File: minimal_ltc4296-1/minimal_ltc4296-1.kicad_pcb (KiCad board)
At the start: 4 copper layers, 71.1 x 50.8 mm, 44 parts, among them J1 TBP02R1-381-03BE, J2 TBP02R1-381-03BE, J3 TBP02R1-381-03BE, J4 TBP02R1-381-03BE, J5 TBP02R1-381-03BE, J6 TBP02R1-381-02BE, Q1 100.0 V, Q2 100.0 V, Q3 100.0 V, Q4 100.0 V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

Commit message: Update KiCad PCB file
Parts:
- moved J6 37.1 mm to (149.7, 118.2), turned to 180 degrees
- moved D1 5.21 mm to (137.8, 106.6), turned to 0 degrees
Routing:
- net GND: vias 40 -> 38
- net /PSE: vias 18 -> 16
- net /OUTM4: vias 2 -> 6
- net /OUTM3: vias 2 -> 6
- net /OUTM2: vias 2 -> 6
- net /OUTM1: vias 2 -> 6
- net /OUTM0: vias 2 -> 6
- added copper zone on B.Cu, net /OUTM0
- added copper zone on B.Cu, net /OUTM1
- added copper zone on B.Cu, net /OUTM2
- added copper zone on B.Cu, net /OUTM3
- added copper zone on B.Cu, net /OUTM4
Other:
- board size 71.1 x 50.8 mm -> 71.1 x 53.3 mm

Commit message: Update KiCad PCB file
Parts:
- moved R14 28.0 mm to (136.3, 89.9), turned to 90 degrees
- moved D2 27.5 mm to (131.1, 89.4), turned to -90 degrees
- moved R12 24.7 mm to (141.1, 89.9), turned to 90 degrees
- moved R11 24.4 mm to (161.6, 89.9), turned to 90 degrees
- moved R10 21.4 mm to (154.8, 89.9), turned to 90 degrees
- moved R13 20.1 mm to (150.0, 89.9), turned to 90 degrees
- moved R15 7.18 mm to (162.6, 84.2)
- moved Q5 7.18 mm to (135.2, 79.2)
- moved R18 7.18 mm to (135.2, 84.2)
- moved Q2 7.12 mm to (162.6, 79.2)
- moved R16 5.68 mm to (155.8, 84.2)
- moved Q3 5.68 mm to (155.8, 79.2)
- moved Q6 5.68 mm to (142.1, 79.2)
- moved R19 5.68 mm to (142.1, 84.2)
- moved Q4 5.08 mm to (148.9, 79.2)
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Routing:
- net /PSE: track 52.0 -> 84.1 mm
- net /LSNS: track 46.1 -> 69.0 mm
- net /OUTM1: track 17.6 -> 31.0 mm, vias 6 -> 2
- net /OUTM0: track 17.8 -> 28.9 mm, vias 6 -> 2
- net /OUTM2: track 13.7 -> 22.8 mm, vias 6 -> 2
- net /HSNSM4: track 11.4 -> 20.0 mm
- net /HGATE4: track 23.8 -> 32.3 mm
- net /OUTP4: track 23.7 -> 32.2 mm
- net /HSNSM0: track 12.4 -> 19.6 mm
- net /OUTP0: track 20.7 -> 27.9 mm
- net /HGATE0: track 22.6 -> 29.8 mm
- net /HSNSM1: track 8.66 -> 14.9 mm
- net /OUTM3: track 16.3 -> 22.5 mm, vias 6 -> 2
- net /HSNSM3: track 8.52 -> 14.6 mm
- net /OUTP2: track 18.3 -> 23.4 mm
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
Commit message: Update KiCad PCB file
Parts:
- moved D2 33.3 mm to (164.5, 89.4)
- moved Q2 3.05 mm to (159.6, 79.2)
- moved Q5 3.05 mm to (138.3, 79.2)
- moved R15 3.05 mm to (159.6, 84.2)
- moved R18 3.05 mm to (138.3, 84.2)
- moved R12 2.54 mm to (143.6, 89.9)
- moved R11 2.03 mm to (159.6, 89.9)
- moved R14 2.03 mm to (138.3, 89.9)
- moved Q3 1.52 mm to (154.3, 79.2)
- moved Q6 1.52 mm to (143.6, 79.2)
- moved R16 1.52 mm to (154.3, 84.2)
- moved R19 1.52 mm to (143.6, 84.2)
- moved R13 1.02 mm to (148.9, 89.9)
- moved R10 0.51 mm to (154.3, 89.9)
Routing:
- net /PSE: track 84.1 -> 78.1 mm
- net /OUTM0: track 28.9 -> 26.1 mm, vias 2 -> 4
- net /OUTM4: track 20.9 -> 18.2 mm, vias 2 -> 4
- net /OUTM1: track 31.0 -> 28.3 mm, vias 2 -> 4
- net /LSNS: track 69.0 -> 66.4 mm
- net /HGATE4: track 32.3 -> 30.1 mm
- net /HGATE0: track 29.8 -> 28.1 mm
- net /HSNSM4: track 20.0 -> 18.7 mm
- net /HSNSM0: track 19.6 -> 18.3 mm
- net /OUTP4: track 32.2 -> 31.0 mm
- net /OUTP1: track 23.6 -> 24.7 mm
- net /OUTM2: track 22.8 -> 21.8 mm, vias 2 -> 4
- net /OUTM3: track 22.5 -> 21.6 mm, vias 2 -> 4
- net /HGATE2: track 24.3 -> 23.5 mm
- net /OUTP0: track 27.9 -> 27.2 mm
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
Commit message: Update KiCad project files
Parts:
- moved D2 2.54 mm to (164.5, 91.9)
- moved R10 2.54 mm to (154.3, 92.4)
- moved R11 2.54 mm to (159.6, 92.4)
- moved R12 2.54 mm to (143.6, 92.4)
- moved R13 2.54 mm to (148.9, 92.4)
- moved R14 2.54 mm to (138.3, 92.4)
- moved C1 0.15 mm to (143.4, 102.1)
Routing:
- net /LSNS: track 66.4 -> 58.9 mm
- net /OUTP0: track 27.2 -> 24.0 mm
- net /OUTP4: track 31.0 -> 27.8 mm
- net /OUTP2: track 23.6 -> 20.4 mm
- net /OUTP1: track 24.7 -> 21.5 mm
- net /OUTP3: track 24.5 -> 21.6 mm
- net /OUTM2: track 21.8 -> 19.3 mm
- net /OUTM4: track 18.2 -> 15.7 mm
- net /OUTM3: track 21.6 -> 19.0 mm
- net /OUTM1: track 28.3 -> 25.9 mm
- net /OUTM0: track 26.1 -> 23.8 mm
- net /PSE: track 78.1 -> 77.2 mm
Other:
- outline, holes or cut-outs redrawn

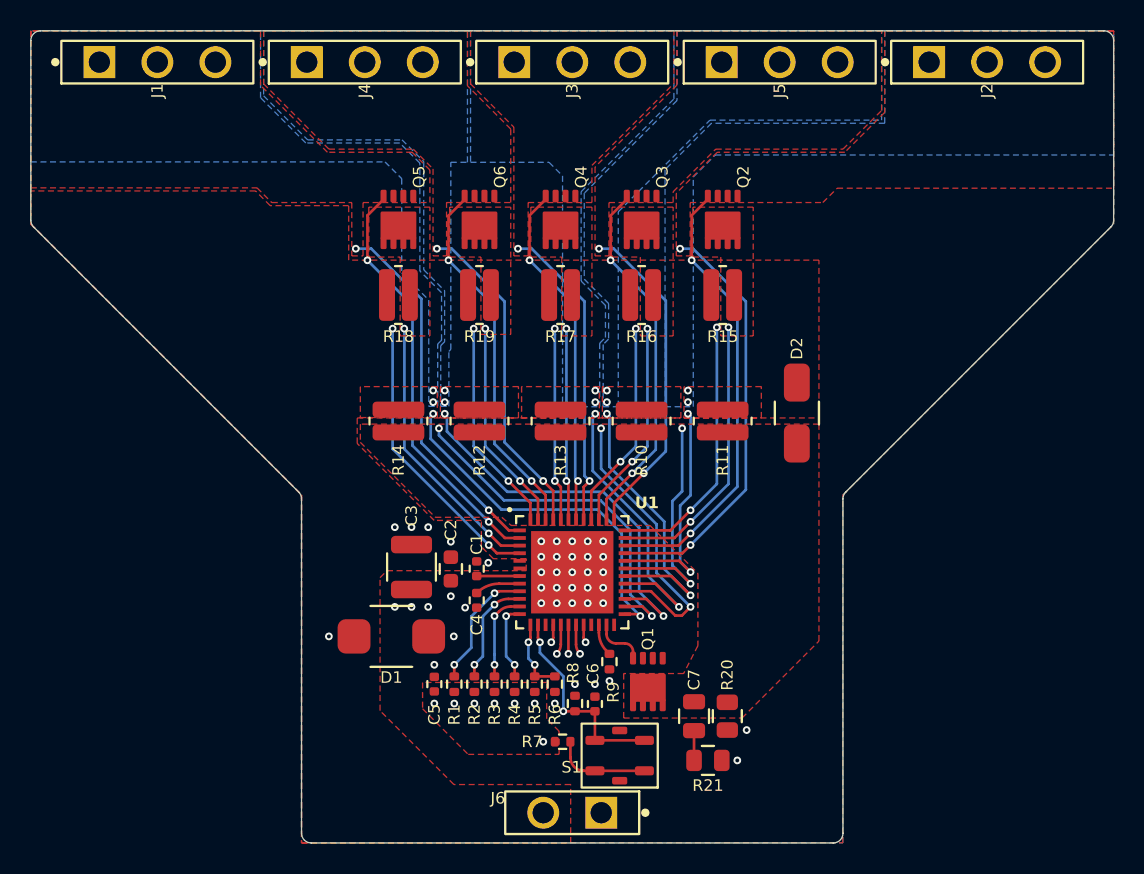
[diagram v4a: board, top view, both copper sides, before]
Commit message: Update KiCad project settings and PCB layout
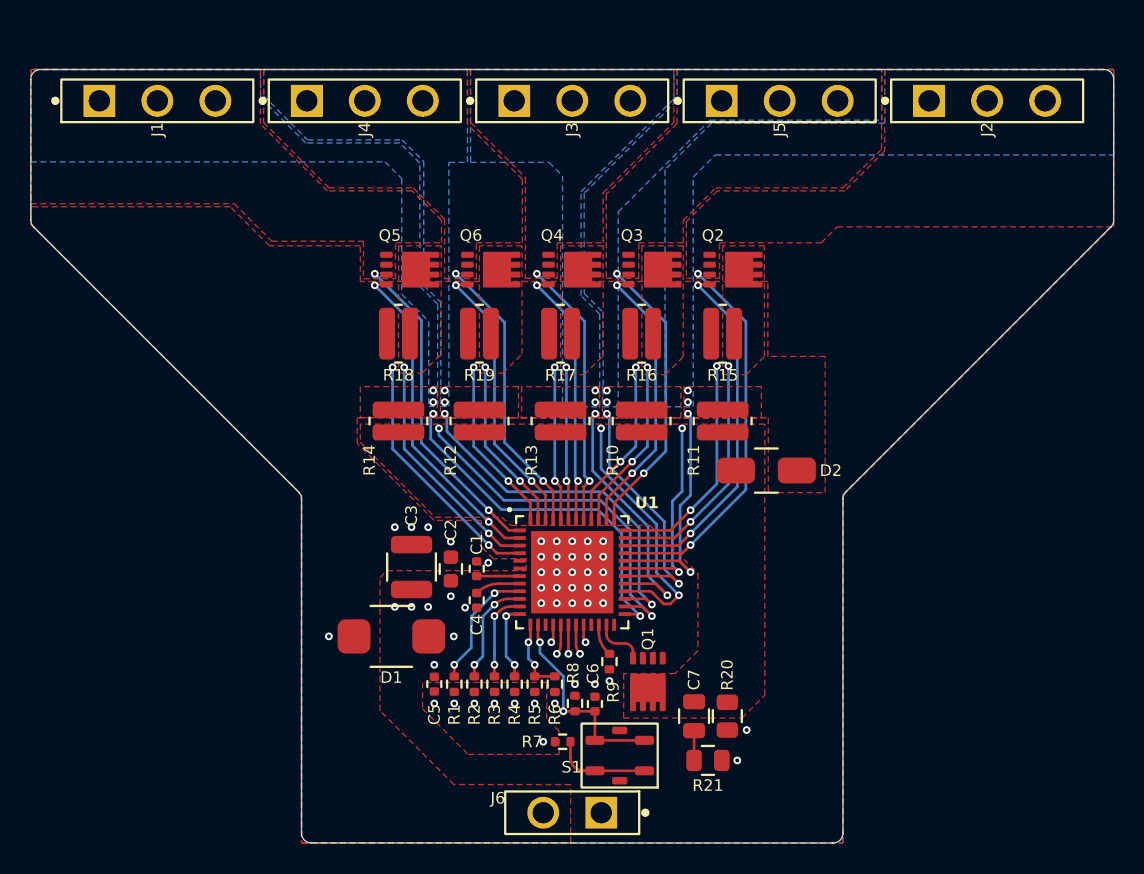
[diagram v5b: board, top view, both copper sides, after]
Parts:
- moved D2 4.28 mm to (162.5, 95.7), turned to 180 degrees
- moved Q5 3.38 mm to (139.0, 82.5), turned to 0 degrees
- moved Q6 3.38 mm to (144.4, 82.5), turned to 0 degrees
- moved Q4 3.38 mm to (149.7, 82.5), turned to 0 degrees
- moved Q3 3.36 mm to (154.9, 82.5), turned to 0 degrees
- moved Q2 3.36 mm to (160.3, 82.5), turned to 0 degrees
- moved J1 2.54 mm to (122.5, 71.4)
- moved J2 2.54 mm to (177.0, 71.4)
- moved J3 2.54 mm to (149.7, 71.4)
- moved J4 2.54 mm to (136.1, 71.4)
- moved J5 2.54 mm to (163.3, 71.4)
- moved R15 2.54 mm to (159.6, 86.7)
- moved R16 2.54 mm to (154.3, 86.7)
- moved R17 2.54 mm to (148.9, 86.7)
- moved R18 2.54 mm to (138.3, 86.7)
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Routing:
- net /PSE: track 77.2 -> 64.5 mm
- net /HGATE0: track 27.6 -> 21.9 mm
- net /HGATE1: track 24.3 -> 18.6 mm
- net /HGATE2: track 23.1 -> 17.3 mm
- net /HGATE4: track 29.8 -> 24.1 mm
- net /HGATE3: track 24.3 -> 18.6 mm
- net /LSNS: track 58.9 -> 54.6 mm
- net /OUTP0: track 24.0 -> 21.2 mm
- net /OUTP1: track 21.5 -> 18.8 mm
- net /OUTP3: track 21.6 -> 18.9 mm
- net /OUTP2: track 20.4 -> 17.7 mm
- net /OUTP4: track 27.8 -> 25.2 mm
- net /HSNSM1: track 14.0 -> 11.4 mm
- net /HSNSM4: track 18.6 -> 16.0 mm
- net /HSNSM3: track 13.9 -> 11.4 mm
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- removed copper zone on In1.Cu, net /PSE
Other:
- board size 71.1 x 53.3 mm -> 71.1 x 50.8 mm

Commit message: Update KiCad PCB file
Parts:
- moved D2 25.3 mm to (137.2, 96.9), turned to 0 degrees
- moved Q3 1.47 mm to (155.0, 84.0), turned to -90 degrees
- moved Q2 1.47 mm to (160.4, 84.0), turned to -90 degrees
- moved Q4 1.47 mm to (149.7, 84.0), turned to -90 degrees
- moved Q5 1.47 mm to (139.1, 84.0), turned to -90 degrees
- moved Q6 1.47 mm to (144.4, 84.0), turned to -90 degrees
- moved R18 1.35 mm to (139.1, 87.8), turned to 90 degrees
- moved R19 1.35 mm to (144.4, 87.8), turned to 90 degrees
- moved R17 1.35 mm to (149.7, 87.8), turned to 90 degrees
- moved R16 1.35 mm to (155.0, 87.8), turned to 90 degrees
- moved R15 1.35 mm to (160.4, 87.8), turned to 90 degrees
- moved R10 0.77 mm to (155.0, 92.4)
- moved R11 0.77 mm to (160.4, 92.4)
- moved R12 0.77 mm to (144.4, 92.4)
- moved R13 0.77 mm to (149.7, 92.4)
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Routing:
- net /PSE: track 64.5 -> 72.4 mm
- net /HSNSM3: track 11.4 -> 15.5 mm
- net /HSNSM4: track 16.0 -> 19.4 mm
- net /HSNSM2: track 10.1 -> 13.2 mm
- net /OUTP1: track 18.8 -> 16.0 mm
- net /OUTP4: track 25.2 -> 22.6 mm
- net /HGATE2: track 17.3 -> 19.5 mm
- net /OUTP0: track 21.2 -> 19.1 mm
- net /OUTM2: track 17.1 -> 15.4 mm
- net /HSNSM0: track 15.6 -> 17.0 mm
- net /OUTP3: track 18.9 -> 17.5 mm
- net /HGATE0: track 21.9 -> 23.2 mm
- net /HGATE1: track 18.6 -> 19.9 mm
- net /OUTM4: track 15.7 -> 14.4 mm
- net /LSNS: track 54.6 -> 54.0 mm
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
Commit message: Update PCB file
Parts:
- moved Q2 1.52 mm to (161.9, 84.0)
- moved Q5 1.52 mm to (137.5, 84.0)
- moved R11 1.52 mm to (161.9, 92.4)
- moved R14 1.52 mm to (137.5, 92.4)
- moved R15 1.52 mm to (161.9, 87.8)
- moved R18 1.52 mm to (137.5, 87.8)
- moved Q3 0.76 mm to (155.8, 84.0)
- moved Q6 0.76 mm to (143.6, 84.0)
- moved R10 0.76 mm to (155.8, 92.4)
- moved R12 0.76 mm to (143.6, 92.4)
- moved R16 0.76 mm to (155.8, 87.8)
- moved R19 0.76 mm to (143.6, 87.8)
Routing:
- net /PSE: track 72.4 -> 74.5 mm
- net /HSNSM3: track 15.5 -> 16.3 mm
- net /LSNS: track 54.0 -> 54.6 mm
- net /OUTP4: track 22.6 -> 23.2 mm
- net /HSNSM0: track 17.0 -> 17.6 mm

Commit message: Update KiCad PCB file
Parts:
- moved D2 2.03 mm to (139.1, 96.4)
- moved D1 0.51 mm to (138.3, 106.6)
- moved C2 0.25 mm to (142.0, 102.1)
- moved C3 0.25 mm to (139.4, 102.0)
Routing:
- net GND: vias 38 -> 148
- added copper zone on In1.Cu, net /OUTM0
- added copper zone on In1.Cu, net /OUTM1
- added copper zone on In1.Cu, net /OUTM2
- added copper zone on In1.Cu, net /OUTM3
- added copper zone on In1.Cu, net /OUTM4
- removed copper zone on B.Cu, net /OUTM0
- removed copper zone on B.Cu, net /OUTM1
- removed copper zone on B.Cu, net /OUTM2
- removed copper zone on B.Cu, net /OUTM3
- removed copper zone on B.Cu, net /OUTM4
